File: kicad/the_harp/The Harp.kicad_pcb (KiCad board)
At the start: 4 copper layers, 56 x 94.5 mm, 181 parts, among them IC501 AK4621EF, J401 PJ-063AH, J402 NMJ6HCD2, J403 NMJ6HCD2, J404 NMJ6HCD2, J405 Bypass FSW, J406 NMJ6HCD2, J407 Hold FSW, J408 OLED 0.91 128x32, K401 G6K-2F-Y, Q401 2N7002, Q402 2N7002, Q403 2N7002, SW101 100-DP6, SW102 100-DP6, SW103 100-DP6, U201 STM32H750VBT6, U202 W25Q128JVSIQ, U301 TPS54202DDC, U302 NCP718ASN500T1G, U401 MCP6001T-I/OT, U501 OPA2348AIDR, U601 THS4522IPW, U701 OPA2365AIDR, U702 OPA1688IDR, Y201 25MHz 9pF

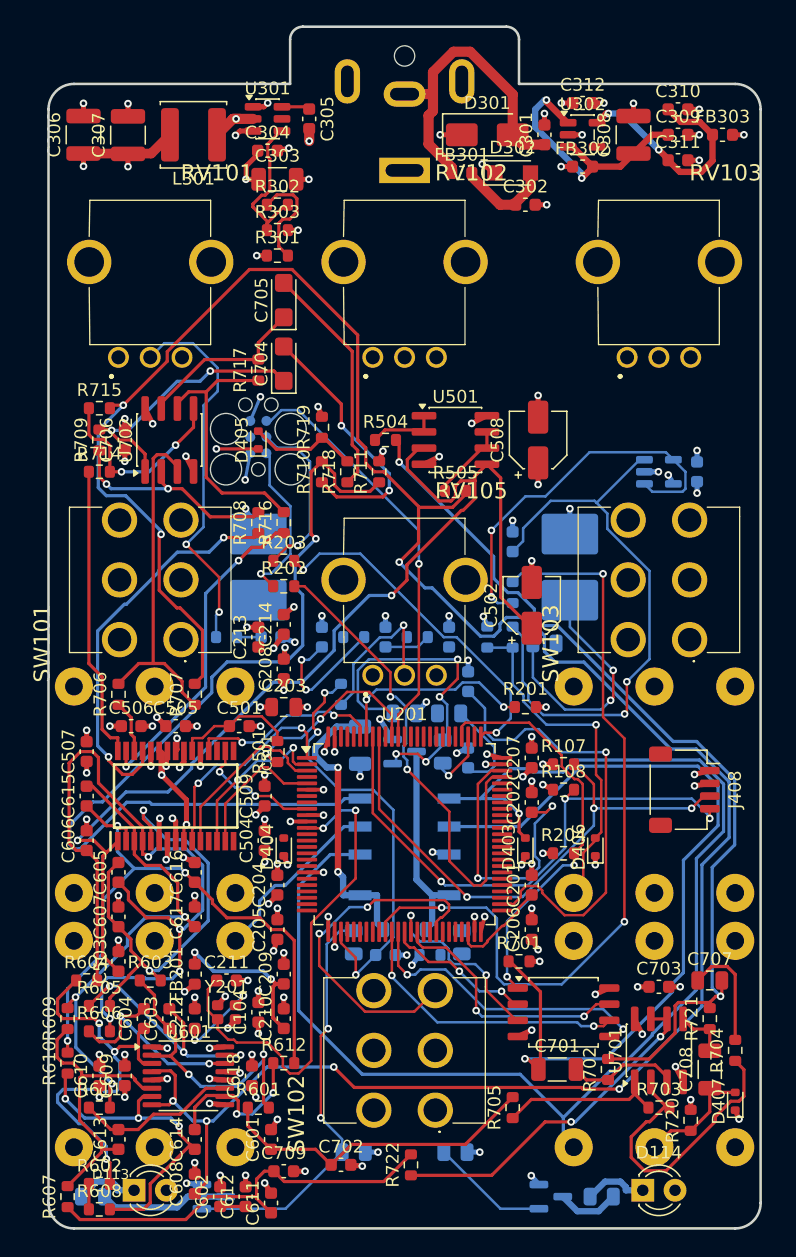
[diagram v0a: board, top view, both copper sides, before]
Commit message: Power section re-placed and re-routed, Alchemist widths, 0/45/90 everywhere
The buck placement from 6a5f05a stays. power.py re-places and routes the
rest of the power section: the DC input on one bus at y = 56 (TVS hanging
off it, FB301 with its two caps under its pads, D302, +9V straight down to
the LDO and onto In2) and the LDO in a second row at y = 63 flowing back
towards the +5V via, input parts at the input, output caps together at the
output. The buck's feedback divider moves to a column beside the FB pin;
the SW node to the BOOT cap crosses on a short B.Cu link instead of In2.

rail.py joins the one open +5V connection on In2, hopping the +3V3 and
+9V rails with two via pairs. widths.py brings every track to the
Alchemist widths, 1.0 / 0.762 / 0.508 / 0.254 (NRST 0.1016), stepping down
where the clearance will not allow it, and re-draws every odd-angle segment
as an orthogonal plus a 45 degree piece. Net classes in the project carry
the same widths and 0.1524 clearance; nets.py knows KiCad's Net-(...)
names.

1623 tracks, 294 vias, no violations in check.py, 29 connections open
(signals and VDDA). Docs and the routing image updated.

Co-Authored-By: Claude Fable 5.1 <noreply@anthropic.com>
Claude-Session: https://claude.ai/code/session_016hDejPHPgG8auBLMyByYZK
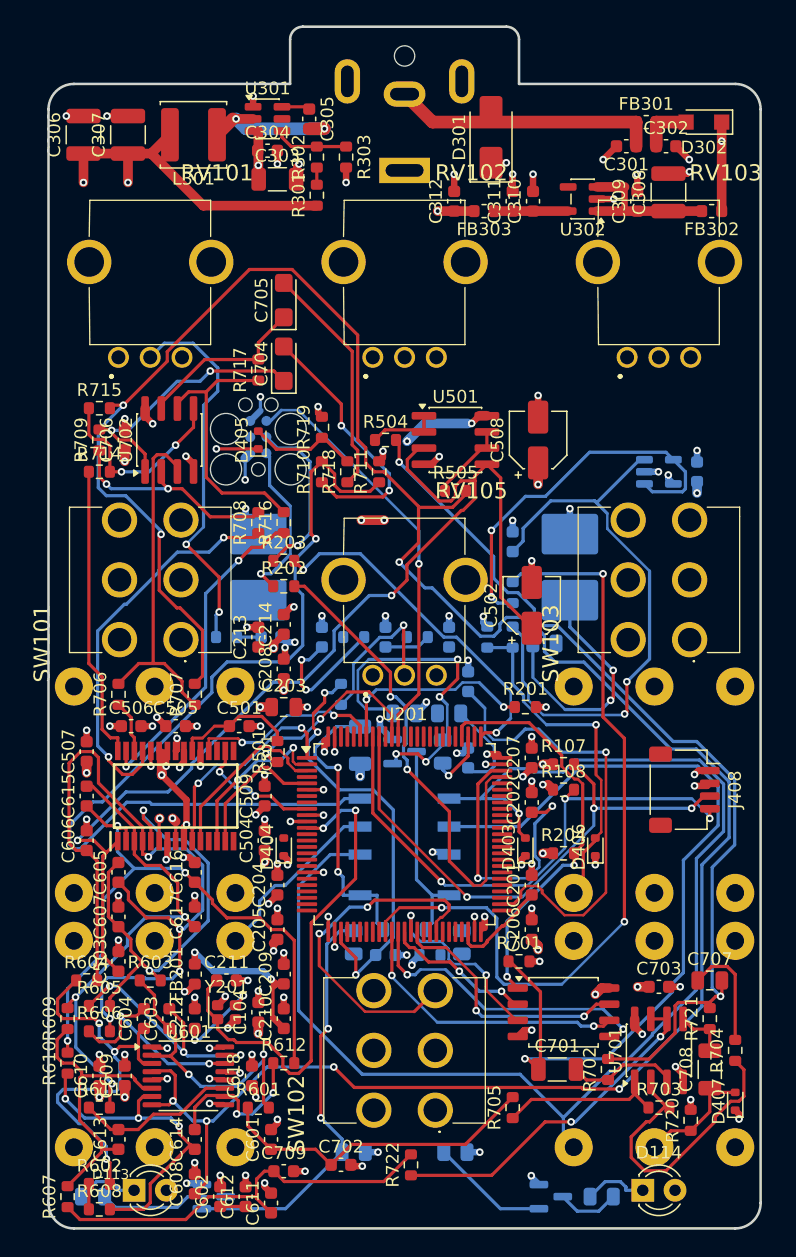
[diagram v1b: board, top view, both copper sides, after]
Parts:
- moved FB303 19.7 mm to (154.8, 63.0), turned to 180 degrees
- moved D302 15.6 mm to (172.0, 56.0), turned to 180 degrees
- moved FB301 15.0 mm to (167.5, 56.0)
- moved C310 13.5 mm to (158.6, 62.2), turned to 90 degrees
- moved C311 13.4 mm to (157.0, 62.2), turned to 90 degrees
- moved C312 12.7 mm to (152.4, 62.2), turned to 90 degrees
- moved C302 12.0 mm to (169.1, 57.9)
- moved FB302 10.7 mm to (172.7, 63.0), turned to 180 degrees
- moved R303 7.89 mm to (143.9, 58.8), turned to -90 degrees
- moved C301 6.50 mm to (165.9, 57.9), turned to 180 degrees
- moved C309 6.13 mm to (166.8, 62.2), turned to 90 degrees
- moved R301 5.67 mm to (141.6, 61.8), turned to 90 degrees
- moved C308 5.30 mm to (169.2, 61.5)
- moved U302 5.05 mm to (162.5, 62.0), turned to 180 degrees
- moved R302 4.87 mm to (141.6, 58.8), turned to 90 degrees
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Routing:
- net +3V3: track 327.4 -> 344.4 mm, vias 33 -> 32
- net +9V: track 237.8 -> 251.6 mm, vias 5 -> 3
- net Net-(U302-OUT): track 18.0 -> 5.83 mm, vias 2 -> 0
- net Net-(U302-EN): track 21.4 -> 12.3 mm, vias 2 -> 0
- net +5V: track 198.9 -> 207.9 mm, vias 19 -> 21
- net Net-(R301-Pad2): track 8.49 -> 1.35 mm
- net GND: track 113.3 -> 120.2 mm
- net Net-(U301-FB): track 12.1 -> 5.84 mm
- net Net-(D301-A2): track 25.4 -> 21.0 mm
- net Net-(D302-A): track 7.62 -> 4.25 mm
